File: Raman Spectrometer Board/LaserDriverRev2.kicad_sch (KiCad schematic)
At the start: 30 parts, among them J6 Conn_01x02, Q5 2N7002, Q6 DMG2301L, U3 LT1009, U4 OPA4192

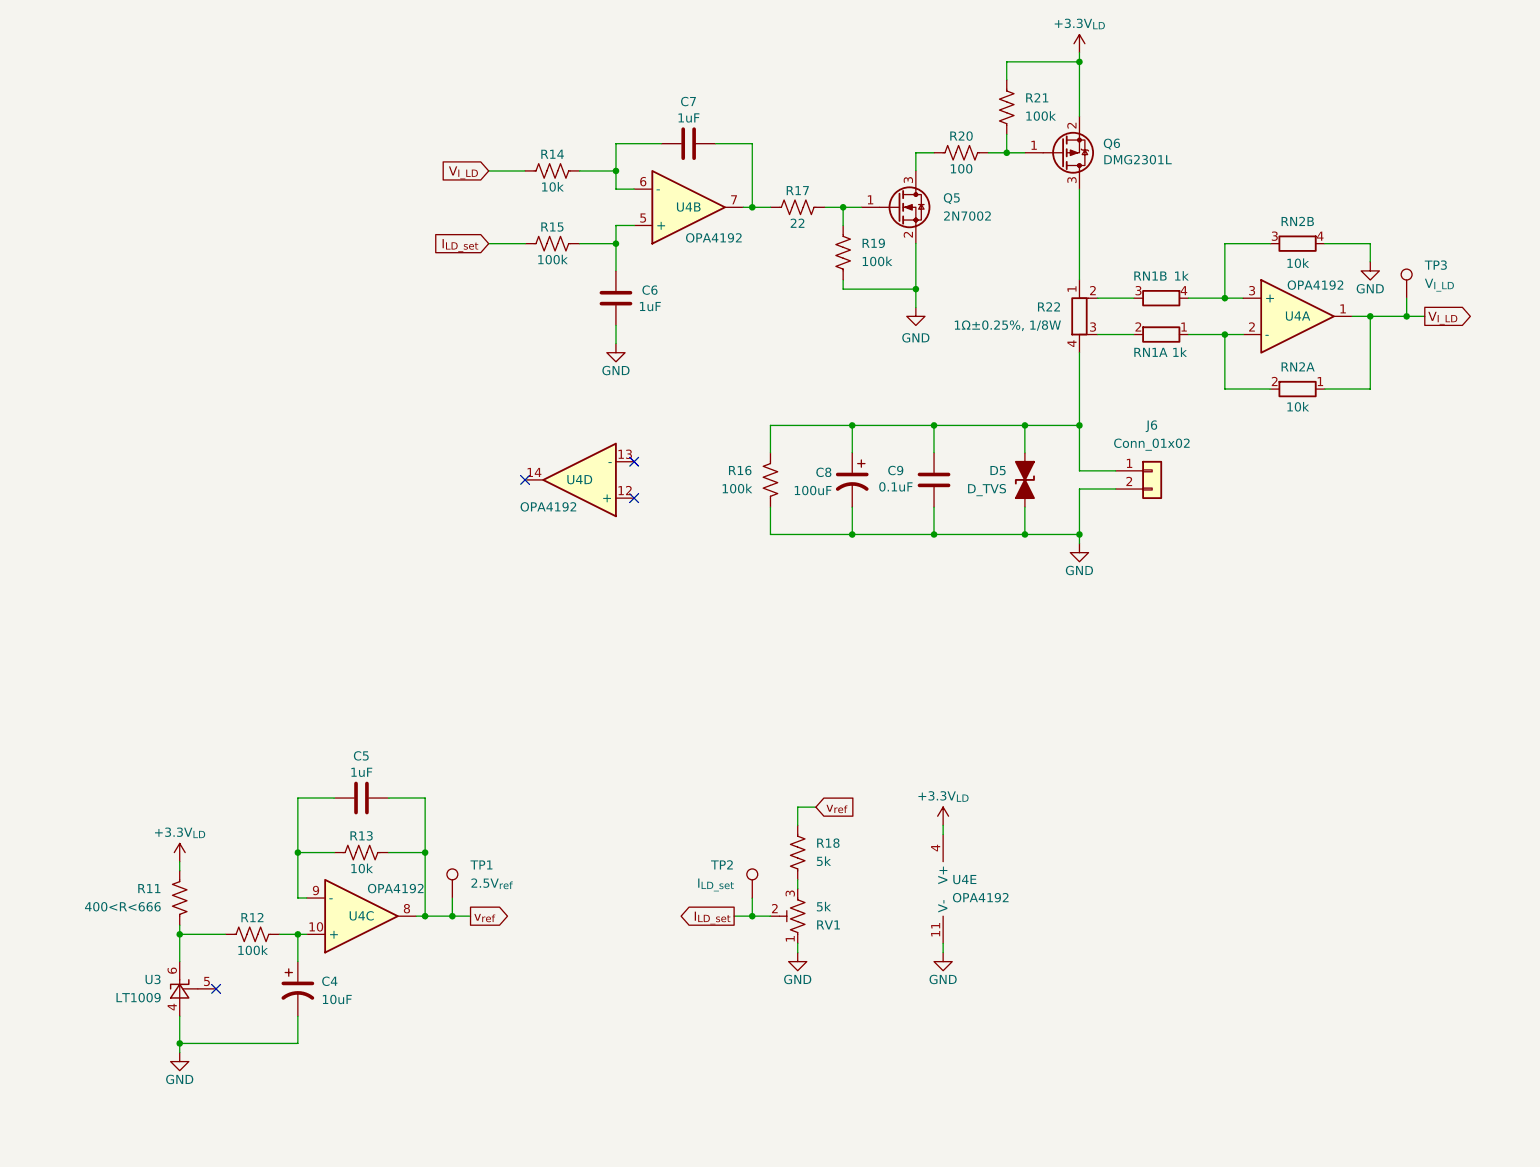
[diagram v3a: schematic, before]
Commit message: Finished laser diode layout
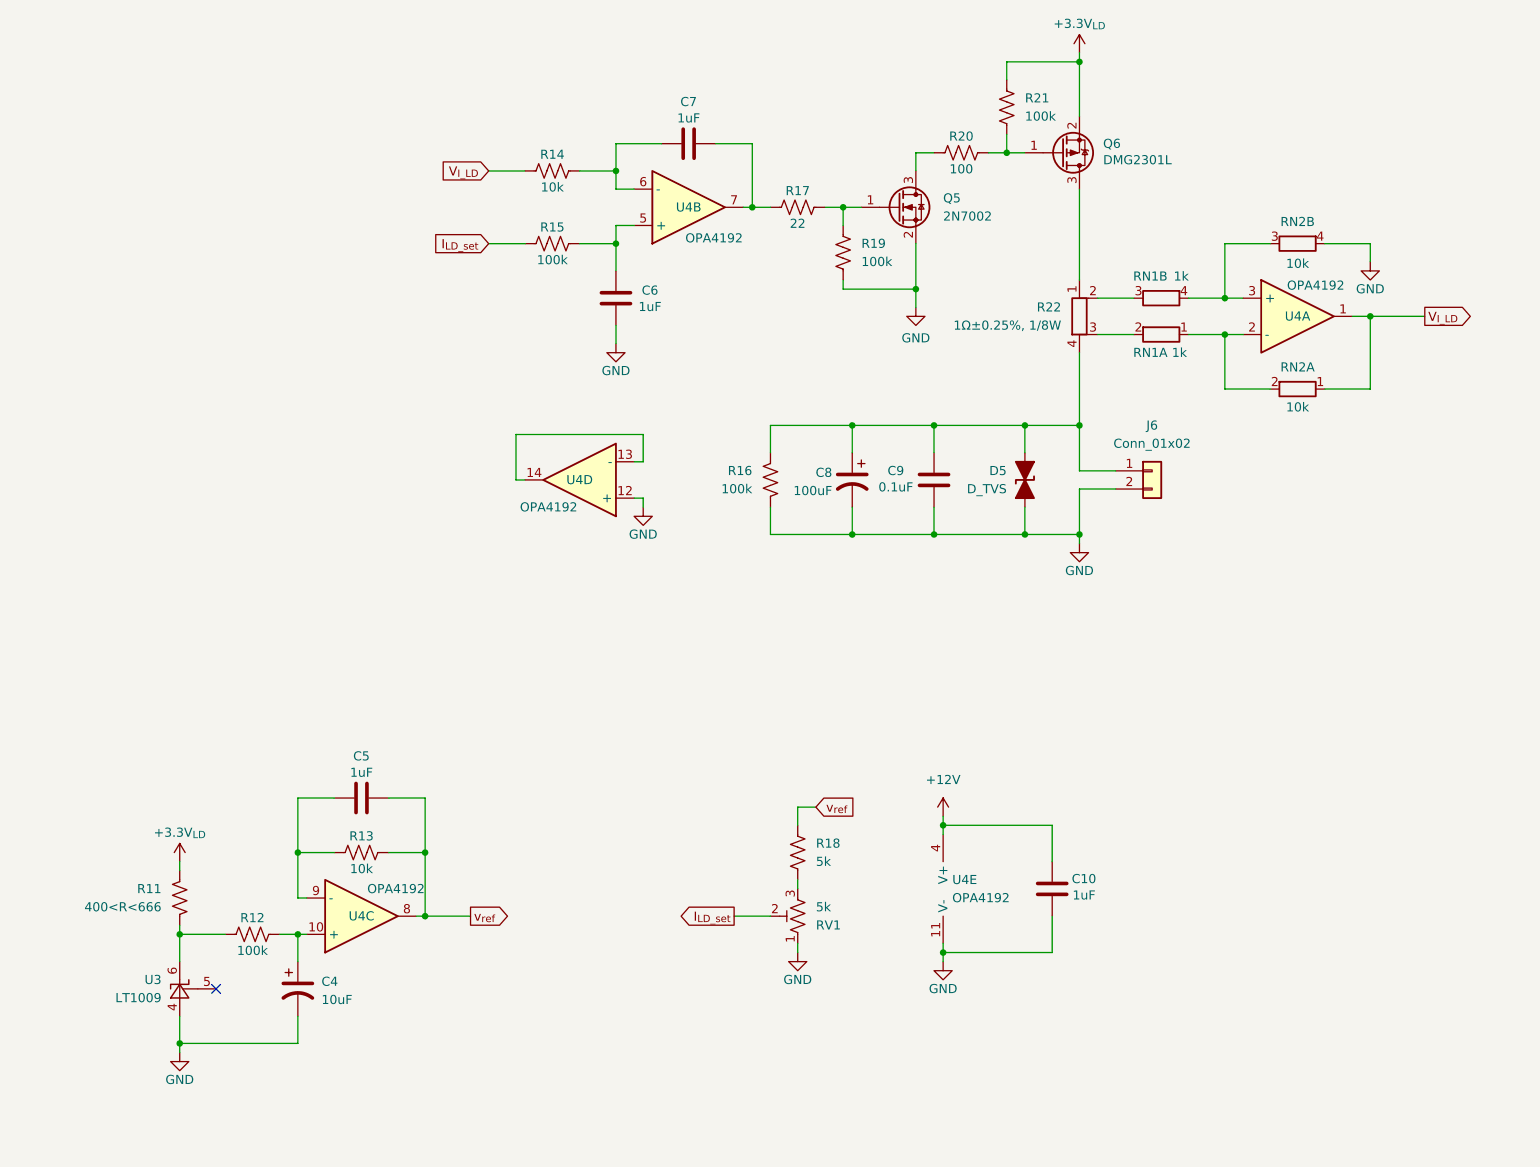
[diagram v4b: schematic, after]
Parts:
- removed TP1: 2.5V_{ref}, TestPoint:TestPoint_Pad_D1.5mm, symbol Connector:TestPoint
- removed TP2: I_{LD_set}, TestPoint:TestPoint_Pad_D1.5mm, symbol Connector:TestPoint
- removed TP3: V_{I_LD}, TestPoint:TestPoint_Pad_D1.5mm, symbol Connector:TestPoint
- added C10: 1uF, Capacitor_SMD:C_0603_1608Metric, symbol Device:C
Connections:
- net +3.3V_{LD}: no longer U4.4 (V+)
- net GND: now also U4.12 (+), C10.2
- net at U4.13 (-): now also U4.14
- new net +12V: C10.1, U4.4 (V+)
- no-connect marks 4 -> 1
